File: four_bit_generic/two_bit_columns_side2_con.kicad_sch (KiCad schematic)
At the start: 2 parts

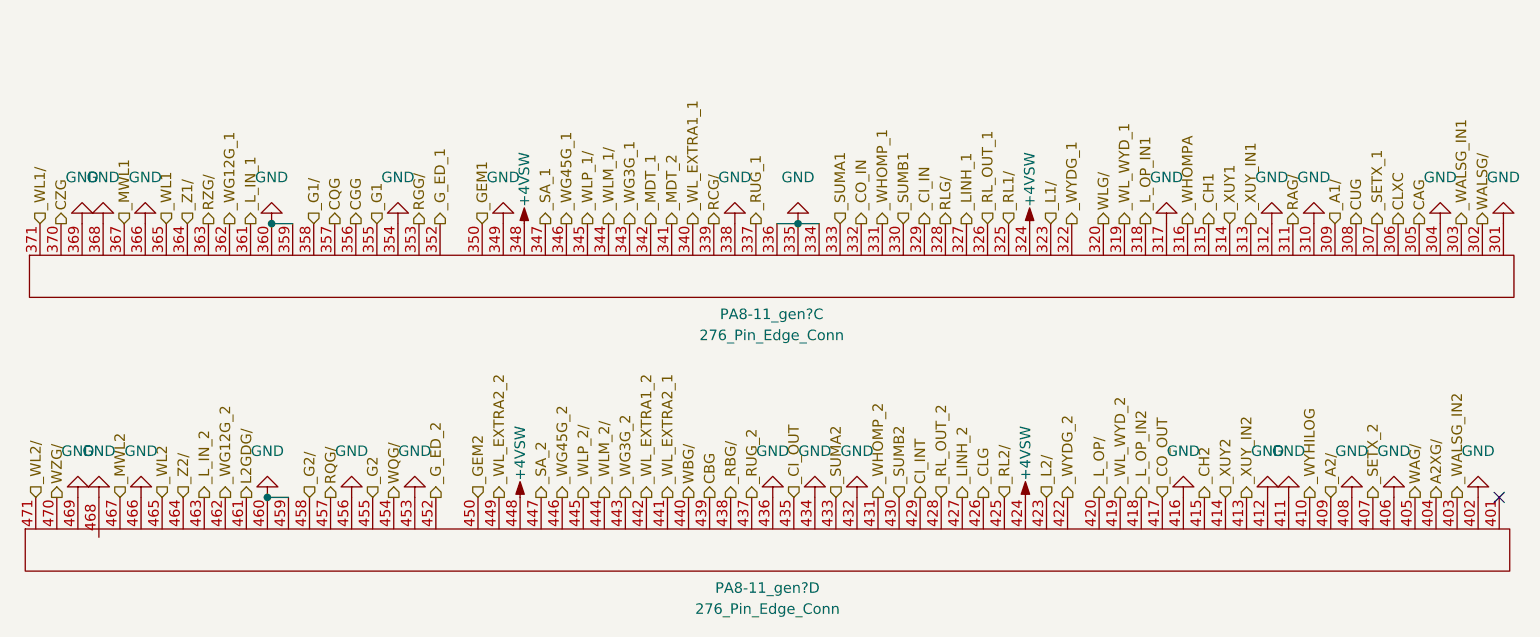
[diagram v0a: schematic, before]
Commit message: Generic  4 Bit Adder schematic + pcb
PCB and schematic updates
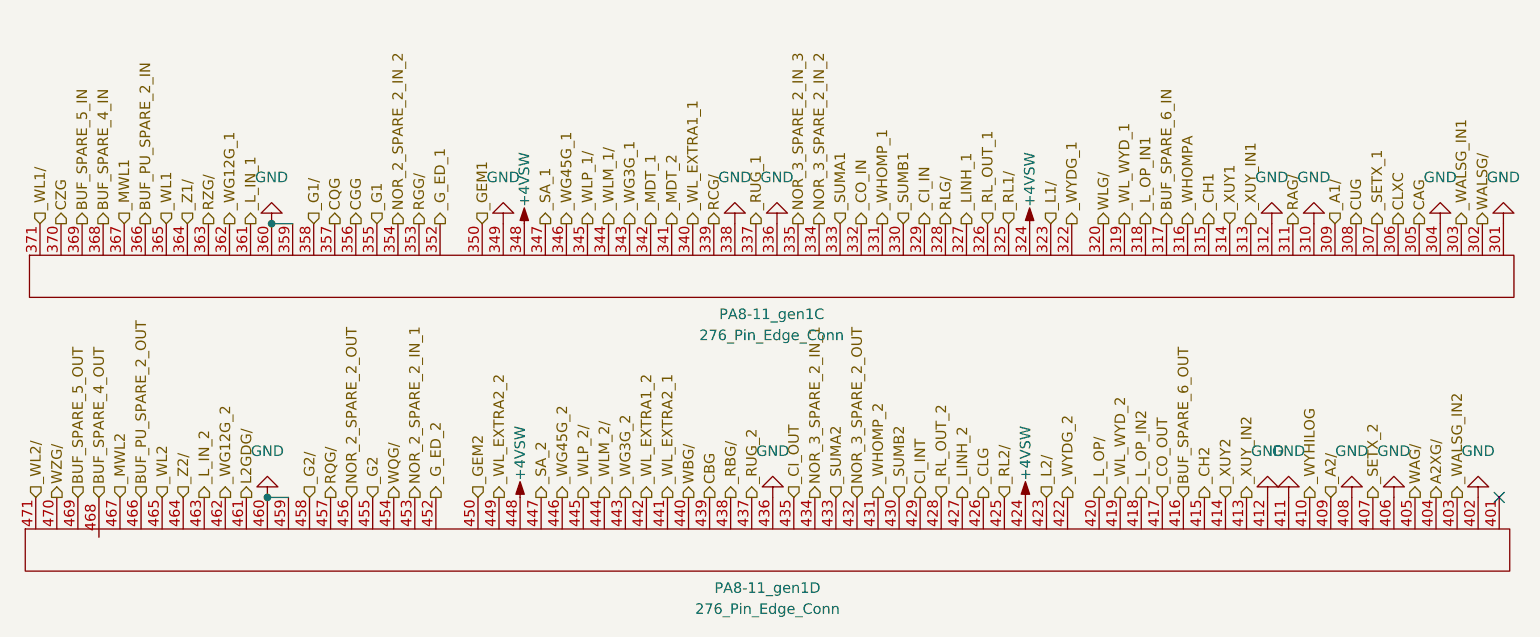
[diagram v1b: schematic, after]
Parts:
- gave numbers to parts that had none: 1
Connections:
- net GND: no longer PA8-11_gen1.317, PA8-11_gen1.334, PA8-11_gen1.335, PA8-11_gen1.354, PA8-11_gen1.366, PA8-11_gen1.368, PA8-11_gen1.369, PA8-11_gen1.416, PA8-11_gen1.432, PA8-11_gen1.434, PA8-11_gen1.453, PA8-11_gen1.456, PA8-11_gen1.466, PA8-11_gen1.468, PA8-11_gen1.469
- new net BUF_PU_SPARE_2_IN: PA8-11_gen1.366
- new net BUF_PU_SPARE_2_OUT: PA8-11_gen1.466
- new net BUF_SPARE_4_IN: PA8-11_gen1.368
- new net BUF_SPARE_4_OUT: PA8-11_gen1.468
- new net BUF_SPARE_5_IN: PA8-11_gen1.369
- new net BUF_SPARE_5_OUT: PA8-11_gen1.469
- new net BUF_SPARE_6_IN: PA8-11_gen1.317
- new net BUF_SPARE_6_OUT: PA8-11_gen1.416
- new net NOR_2_SPARE_2_IN_1: PA8-11_gen1.453
- new net NOR_2_SPARE_2_IN_2: PA8-11_gen1.354
- new net NOR_2_SPARE_2_OUT: PA8-11_gen1.456
- new net NOR_3_SPARE_2_IN_1: PA8-11_gen1.434
- new net NOR_3_SPARE_2_IN_2: PA8-11_gen1.334
- new net NOR_3_SPARE_2_IN_3: PA8-11_gen1.335
- new net NOR_3_SPARE_2_OUT: PA8-11_gen1.432
